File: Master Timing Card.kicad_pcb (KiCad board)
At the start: 4 copper layers, 170 x 100 mm, 412 parts, among them CN1 M20-9990346, CN10 M2 x 2.5mm, CN11 UE75-A20-6000T, CN12 U77-A1114-30L1, CN13 Harwin M20-9990246, CN14 USB4110-GF-A, CN15 731385033, CN2 Samtec GRF1-J-P-08-E-RA-TH1, CN3 Amphenol 86093488613755E1LF, CN6 SQW-104-01-F-D-VS, CN7 104031-0811, CN9 TE 1-2199230-6, J1 Connector_RJ45_Magjack_Abraco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, Q1 DMN62D0U-7, Q2 DMN62D0U-7, Q3 DMN62D0U-7, Q4 onsemi FDC6330L, Q5 TSM085P03CV RGG, Q6 DMN62D0U-7, T1 TC2-72T+, T2 TC2-72T+, T3 TC2-72T+, T4 TC2-72T+, T5 TC2-72T+, T6 TC2-72T+, T7 TC2-72T+, T8 TC2-72T+, T9 TC2-72T+, U1 Microchip 24LC024-E/MC, U10 INA3221AIRGV, U11 SY75576LKY, U12 TI TPS79301DBV, U13 LT3045IDD#PBF, U14 LT3045IDD#PBF, U15 SN74LVC1G02DCK, U2 Analog MAX3483ESA+, U3 TI TPS79301DBV, U4 TI TPS79301DBV, U5 RC32504A000GNK#BB0, U6 RC32504A000GNK#BB0, U7 SN74LVC1G125DBV, U8 SN74LVC1G125DBV, U9 Analog LT8650SEV#PBF

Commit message: schematic complete
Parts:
- removed C154, C156: 100n, Capacitor_SMD:C_0402_1005Metric
- removed CN1: M20-9990346, Connector_PinHeader_2.54mm:PinHeader_1x03_P2.54mm_Vertical
- removed FB1: 1k8, Inductor_SMD:L_0402_1005Metric
- removed R123, R124: 22k, Resistor_SMD:R_0402_1005Metric
- removed R125, R126: 4k7, Resistor_SMD:R_0402_1005Metric
- removed R127, R128, R132: 100R, Resistor_SMD:R_0402_1005Metric
- added C121: 100n, Capacitor_SMD:C_0402_1005Metric, F.Cu at (233.4, -18.0)
- added C144: 100n, Capacitor_SMD:C_0402_1005Metric, F.Cu at (233.4, -16.0)
- added C159: 100n, Capacitor_SMD:C_0402_1005Metric, F.Cu at (233.4, -14.0)
- added C160: 100n, Capacitor_SMD:C_0402_1005Metric, F.Cu at (246.4, -10.5)
- added C161: 100n, Capacitor_SMD:C_0402_1005Metric, F.Cu at (184.8, 102.8)
- added C162: 100n, Capacitor_SMD:C_0402_1005Metric, F.Cu at (184.8, 112.8)
- added C163: 100n, Capacitor_SMD:C_0402_1005Metric, F.Cu at (184.8, 114.8)
- added C164: 100n, Capacitor_SMD:C_0402_1005Metric, F.Cu at (184.8, 97.8)
- added C165: 100n, Capacitor_SMD:C_0402_1005Metric, F.Cu at (184.8, 99.8)
- added C166: 100n, Capacitor_SMD:C_0402_1005Metric, F.Cu at (184.8, 117.8)
- added C167: 100n, Capacitor_SMD:C_0402_1005Metric, F.Cu at (184.8, 119.8)
- added FB30: 1k8, Inductor_SMD:L_0402_1005Metric, F.Cu at (230.5, -18.0)
- added FB31: 1k8, Inductor_SMD:L_0402_1005Metric, F.Cu at (230.5, -16.0)
- added OSC1: 10MHz, Crystal:Crystal_SMD_3225-4Pin_3.2x2.5mm, F.Cu at (237.4, -16.7)
- added R133: 33R, Resistor_SMD:R_0402_1005Metric, F.Cu at (230.5, -14.0)
- added R134: 33R, Resistor_SMD:R_0402_1005Metric, F.Cu at (230.5, -12.0)
- added R135: 33R, Resistor_SMD:R_0402_1005Metric, F.Cu at (230.5, -10.0)
- added R136: 100R, Resistor_SMD:R_0402_1005Metric, F.Cu at (243.5, -2.50)
- added R137: 10k, Resistor_SMD:R_0402_1005Metric, F.Cu at (230.5, -8.01)
- added U16: SN74LVC2G157DCU, Package_SO:VSSOP-8_2.3x2mm_P0.5mm, F.Cu at (234.7, -11.3)
- R90: value 49R9 -> 100R
- R93: value 49R9 -> 10k
- U1: value Microchip 24LC024-E/MC -> DS2431P+; footprint Package_DFN_QFN:DFN-8-1EP_3x2mm_P0.5mm_EP1.36x1.46mm -> Package_SO_J-Lead:TSOC-6_3.76x3.94mm_P1.27mm
- moved LD9 282.1 mm to (47.7, 40.0), turned to -90 degrees
- moved U6 216.1 mm to (178.5, 111.2)
- moved T8 212.2 mm to (188.8, 118.8), turned to 90 degrees
- moved C111 205.1 mm to (184.8, 92.8), turned to 90 degrees
- moved C114 205.1 mm to (184.8, 94.8), turned to -90 degrees
- moved T7 203.8 mm to (188.8, 98.8), turned to 90 degrees
- moved CN15 202.5 mm to (40.0, 75.0), turned to -90 degrees
- moved C105 202.4 mm to (184.8, 104.8), turned to -90 degrees
- moved C108 202.3 mm to (184.8, 109.8), turned to -90 degrees
- moved T6 199.5 mm to (188.8, 113.8), turned to 90 degrees
- moved T5 192.2 mm to (188.8, 103.8), turned to 90 degrees
- moved R56 185.4 mm to (328.5, 36.7)
- moved C119 185.4 mm to (320.6, 26.1)
- moved C122 185.4 mm to (324.5, 33.9)
- moved LD1 185.4 mm to (338.2, 46.6)
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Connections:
- net /PLL and SFP/OE renamed /PLL and SFP/PLL_OE
- C105 pad 1: 0V -> /PLL and SFP/Frequency Synthesiser 2/RF1_P
- C108 pad 1: 0V -> /PLL and SFP/Frequency Synthesiser 2/RF2_N
- C111 pad 1: 0V -> /PLL and SFP/Frequency Synthesiser 1/RF3_P
- C114 pad 1: 0V -> /PLL and SFP/Frequency Synthesiser 1/RF3_N
- C12 pad 1: /GPS/GNSS_25MHZ -> /GPS/GNSS_CLK
- C153 pad 1: Net-(U13-EN/UV) -> /PLL and SFP/Frequency Synthesiser 1/VIN
- C155 pad 1: Net-(U14-EN/UV) -> /PLL and SFP/Frequency Synthesiser 2/VIN
- C23 pad 1: Net-(Q1-G) -> /GPS/GNSS_RESET
- C26 pad 1: 0V -> /PLL and SFP/Frequency Synthesiser 1/RF1_P
- C29 pad 1: 0V -> /PLL and SFP/Frequency Synthesiser 1/RF2_P
- C3 pad 1: Net-(U1-VCC) -> /PLL and SFP/Frequency Synthesiser 1/RF1_N
- C3 pad 2: 0V -> Net-(C3-Pad2)
- C32 pad 1: 0V -> /PLL and SFP/Frequency Synthesiser 1/RF2_N
- C35 pad 1: 0V -> /PLL and SFP/Frequency Synthesiser 2/RF2_P
- C57 pad 1: /PLL and SFP/Frequency Synthesiser 1/1v8_VDDREF -> /PLL and SFP/Frequency Synthesiser 1/1V8_VDDREF
- C58 pad 1: /PLL and SFP/Frequency Synthesiser 1/1v8_VDDREF -> /PLL and SFP/Frequency Synthesiser 1/1V8_VDDREF
- C83 pad 1: /PLL and SFP/Frequency Synthesiser 2/1v8_VDDREF -> /PLL and SFP/Frequency Synthesiser 2/1V8_VDDREF
- C90 pad 1: /PLL and SFP/Frequency Synthesiser 2/1v8_VDDREF -> /PLL and SFP/Frequency Synthesiser 2/1V8_VDDREF
- CN3 pad a1: Net-(CN3-Pada1) -> /RS485_B
- CN3 pad a10: 0V -> unconnected-(CN3-Pada10)
- CN3 pad a13: /SLOTS_EEPROM_3V3 -> unconnected-(CN3-Pada13)
- CN3 pad a14: /SLOTS_EEPROM_WP -> unconnected-(CN3-Pada14)
- CN3 pad a15: /PSU_EEPROM_SDA -> unconnected-(CN3-Pada15)
- CN3 pad a16: /PSU_EEPROM_ADDR2 -> 0V
- CN3 pad a2: Net-(CN3-Pada1) -> unconnected-(CN3-Pada2)
- CN3 pad a3: 0V -> unconnected-(CN3-Pada3)
- CN3 pad a4: Net-(CN3-Pada4) -> unconnected-(CN3-Pada4)
- CN3 pad a5: Net-(CN3-Pada4) -> unconnected-(CN3-Pada5)
- CN3 pad a6: 0V -> unconnected-(CN3-Pada6)
- CN3 pad a7: Net-(CN3-Pada7) -> unconnected-(CN3-Pada7)
- CN3 pad a8: Net-(CN3-Pada7) -> unconnected-(CN3-Pada8)
- CN3 pad a9: 0V -> unconnected-(CN3-Pada9)
- CN3 pad b1: unconnected-(CN3-Padb1) -> /RS485_A
- CN3 pad b10: 0V -> unconnected-(CN3-Padb10)
- CN3 pad b13: /SLOTS_EEPROM_SDA -> unconnected-(CN3-Padb13)
- CN3 pad b14: /SLOTS_EEPROM_SCL -> unconnected-(CN3-Padb14)
- CN3 pad b15: /PSU_EEPROM_SCL -> unconnected-(CN3-Padb15)
- CN3 pad b16: /PSU_EEPROM_ADDR1 -> unconnected-(CN3-Padb16)
- CN3 pad b3: 0V -> unconnected-(CN3-Padb3)
- CN3 pad b4: Net-(CN3-Padb4) -> unconnected-(CN3-Padb4)
- CN3 pad b5: Net-(CN3-Padb4) -> unconnected-(CN3-Padb5)
- CN3 pad b6: 0V -> unconnected-(CN3-Padb6)
- CN3 pad b7: Net-(CN3-Padb7) -> unconnected-(CN3-Padb7)
- CN3 pad b8: Net-(CN3-Padb7) -> unconnected-(CN3-Padb8)
- CN3 pad b9: 0V -> unconnected-(CN3-Padb9)
- CN3 pad c1: Net-(CN3-Padc1) -> Net-(U1-IO)
- CN3 pad c10: 0V -> unconnected-(CN3-Padc10)
- CN3 pad c13: /RS485_B -> unconnected-(CN3-Padc13)
- CN3 pad c14: /RS485_A -> unconnected-(CN3-Padc14)
- CN3 pad c15: /PSU_EEPROM_3V3 -> unconnected-(CN3-Padc15)
- CN3 pad c16: /PSU_EEPROM_ADDR0 -> unconnected-(CN3-Padc16)
- CN3 pad c2: Net-(CN3-Padc1) -> unconnected-(CN3-Padc2)
- CN3 pad c3: 0V -> unconnected-(CN3-Padc3)
- CN3 pad c4: Net-(CN3-Padc4) -> unconnected-(CN3-Padc4)
- CN3 pad c5: Net-(CN3-Padc4) -> unconnected-(CN3-Padc5)
- CN3 pad c6: 0V -> unconnected-(CN3-Padc6)
- CN3 pad c7: Net-(CN3-Padc7) -> unconnected-(CN3-Padc7)
- CN3 pad c8: Net-(CN3-Padc7) -> unconnected-(CN3-Padc8)
- CN3 pad c9: 0V -> unconnected-(CN3-Padc9)
- CN4 pad 24: unconnected-(CN4D-GPIO26-Pad24) -> Net-(CN4D-GPIO26)
- CN4 pad 48: unconnected-(CN4D-GPIO27-Pad48) -> Net-(CN4D-GPIO27)
- CN6 pad 7: /GPS/GNSS_25MHZ -> /GPS/GNSS_CLK
- CN7 pad 10: unconnected-(CN7-DET_A-Pad10) -> 0V
- FB13 pad 2: /PLL and SFP/Frequency Synthesiser 1/1v8_VDDREF -> /PLL and SFP/Frequency Synthesiser 1/1V8_VDDREF
- FB21 pad 2: /PLL and SFP/Frequency Synthesiser 2/1v8_VDDREF -> /PLL and SFP/Frequency Synthesiser 2/1V8_VDDREF
- FB28 pad 2: Net-(U13-EN/UV) -> /PLL and SFP/Frequency Synthesiser 1/VIN
- FB29 pad 2: Net-(U14-EN/UV) -> /PLL and SFP/Frequency Synthesiser 2/VIN
- FB5 pad 2: /GPS/GNSS_25MHZ -> /GPS/GNSS_CLK
- Q1 pad 1: Net-(Q1-G) -> /GPS/GNSS_RESET
- R17 pad 1: /GPS/GNSS_25MHZ -> Net-(U16-B)
- R24 pad 1: /GPS/GNSS_RESET -> Net-(CN4D-GPIO26)
- R24 pad 2: Net-(Q1-G) -> /GPS/CLK_SEL
- R25 pad 1: Net-(Q1-G) -> /GPS/GNSS_RESET
- R90 pad 1: Net-(U11-IN1_N) -> /GPS/REF_CLK_P
- R90 pad 2: 0V -> /GPS/REF_CLK_N
- R93 pad 1: Net-(U11-IN1_P) -> /PLL and SFP/CLK_SEL
- T1 pad 1: Net-(U5-OUT0_P) -> Net-(C26-Pad2)
- T1 pad 2: Net-(C26-Pad2) -> 0V
- T1 pad 3: Net-(U5-OUT0_N) -> Net-(C3-Pad2)
- T2 pad 1: Net-(U5-OUT1_N) -> Net-(C32-Pad2)
- T2 pad 2: Net-(C29-Pad2) -> 0V
- T2 pad 3: Net-(U5-OUT1_P) -> Net-(C29-Pad2)
- T3 pad 1: Net-(U5-OUT2_N) -> Net-(C108-Pad2)
- T3 pad 2: Net-(C32-Pad2) -> 0V
- T3 pad 3: Net-(U5-OUT2_P) -> Net-(C35-Pad2)
- T3 pad 4: /RF3 -> /RF6
- T4 pad 1: Net-(U5-OUT3_N) -> Net-(C114-Pad2)
- T4 pad 2: Net-(C35-Pad2) -> 0V
- T4 pad 3: Net-(U5-OUT3_P) -> Net-(C111-Pad2)
- T4 pad 4: /RF4 -> /RF3
- T5 pad 1: Net-(U6-OUT0_P) -> Net-(C105-Pad2)
- T5 pad 2: Net-(C105-Pad2) -> 0V
- T5 pad 3: Net-(U6-OUT0_N) -> Net-(C161-Pad2)
- T6 pad 1: Net-(U6-OUT1_N) -> Net-(C163-Pad2)
- T6 pad 2: Net-(C108-Pad2) -> 0V
- T6 pad 3: Net-(U6-OUT1_P) -> Net-(C162-Pad2)
- T6 pad 4: /RF6 -> /RF7
- T7 pad 1: Net-(U6-OUT2_N) -> Net-(C165-Pad2)
- T7 pad 2: Net-(C111-Pad2) -> 0V
- T7 pad 3: Net-(U6-OUT2_P) -> Net-(C164-Pad2)
- T7 pad 4: /RF7 -> /RF4
- T8 pad 1: Net-(U6-OUT3_N) -> Net-(C167-Pad2)
- T8 pad 2: Net-(C114-Pad2) -> 0V
- T8 pad 3: Net-(U6-OUT3_P) -> Net-(C166-Pad2)
- U1 pad 1: /PSU_EEPROM_ADDR0 -> 0V
- U1 pad 2: /PSU_EEPROM_ADDR1 -> Net-(U1-IO)
- U1 pad 3: /PSU_EEPROM_ADDR2 -> unconnected-(U1-NC-Pad3)
- U1 pad 4: 0V -> unconnected-(U1-NC-Pad4)
- U1 pad 5: /PSU_EEPROM_SDA -> unconnected-(U1-NC-Pad5)
- U1 pad 6: /PSU_EEPROM_SCL -> unconnected-(U1-NC-Pad6)
- U11 pad 1: unconnected-(U11-SEL-Pad1) -> /PLL and SFP/CLK_SEL
- U11 pad 3: Net-(U11-IN1_P) -> /GPS/REF_CLK_P
- U11 pad 4: Net-(U11-IN1_N) -> /GPS/REF_CLK_N
- U13 pad 1: Net-(U13-EN/UV) -> /PLL and SFP/Frequency Synthesiser 1/VIN
- U13 pad 2: Net-(U13-EN/UV) -> /PLL and SFP/Frequency Synthesiser 1/VIN
- U13 pad 3: Net-(U13-EN/UV) -> /PLL and SFP/Frequency Synthesiser 1/VIN
- U13 pad 4: Net-(U13-PG) -> unconnected-(U13-PG-Pad4)
- U13 pad 6: Net-(U13-PGFB) -> /PLL and SFP/Frequency Synthesiser 1/VIN
- U14 pad 1: Net-(U14-EN/UV) -> /PLL and SFP/Frequency Synthesiser 2/VIN
- U14 pad 2: Net-(U14-EN/UV) -> /PLL and SFP/Frequency Synthesiser 2/VIN
- U14 pad 3: Net-(U14-EN/UV) -> /PLL and SFP/Frequency Synthesiser 2/VIN
- U14 pad 4: Net-(U14-PG) -> unconnected-(U14-PG-Pad4)
- U14 pad 6: Net-(U14-PGFB) -> /PLL and SFP/Frequency Synthesiser 2/VIN
- U5 pad 11: Net-(U5-OUT3_N) -> /PLL and SFP/Frequency Synthesiser 1/RF4_N
- U5 pad 12: Net-(U5-OUT3_P) -> /PLL and SFP/Frequency Synthesiser 1/RF4_P
- U5 pad 14: Net-(U5-OUT2_N) -> /PLL and SFP/Frequency Synthesiser 1/RF3_N
- U5 pad 15: Net-(U5-OUT2_P) -> /PLL and SFP/Frequency Synthesiser 1/RF3_P
- U5 pad 17: Net-(U5-OUT1_N) -> /PLL and SFP/Frequency Synthesiser 1/RF2_N
- U5 pad 18: Net-(U5-OUT1_P) -> /PLL and SFP/Frequency Synthesiser 1/RF2_P
- U5 pad 20: Net-(U5-OUT0_P) -> /PLL and SFP/Frequency Synthesiser 1/RF1_P
- U5 pad 21: Net-(U5-OUT0_N) -> /PLL and SFP/Frequency Synthesiser 1/RF1_N
- U6 pad 11: Net-(U6-OUT3_N) -> /PLL and SFP/Frequency Synthesiser 2/RF4_N
- U6 pad 12: Net-(U6-OUT3_P) -> /PLL and SFP/Frequency Synthesiser 2/RF4_P
- U6 pad 14: Net-(U6-OUT2_N) -> /PLL and SFP/Frequency Synthesiser 2/RF3_N
- U6 pad 15: Net-(U6-OUT2_P) -> /PLL and SFP/Frequency Synthesiser 2/RF3_P
- U6 pad 17: Net-(U6-OUT1_N) -> /PLL and SFP/Frequency Synthesiser 2/RF2_N
- U6 pad 18: Net-(U6-OUT1_P) -> /PLL and SFP/Frequency Synthesiser 2/RF2_P
- U6 pad 20: Net-(U6-OUT0_P) -> /PLL and SFP/Frequency Synthesiser 2/RF1_P
- U6 pad 21: Net-(U6-OUT0_N) -> /PLL and SFP/Frequency Synthesiser 2/RF1_N
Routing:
- net 0V: track 4.10 -> 45.6 mm, vias 8 -> 37
- net /PSU_EEPROM_SCL: track 12.5 -> 0.00 mm
- net /PLL and SFP/Frequency Synthesiser 1/RF1_N: track 0.00 -> 10.6 mm
- net Net-(U5-OUT0_N): track 10.5 -> 0.00 mm
- net /PSU_EEPROM_ADDR1: track 10.2 -> 0.00 mm
- net /PLL and SFP/Frequency Synthesiser 1/RF1_P: track 0.00 -> 9.85 mm
- net /PLL and SFP/Frequency Synthesiser 1/RF4_N: track 0.00 -> 9.61 mm
- net /PSU_EEPROM_ADDR0: track 9.58 -> 0.00 mm
- net /PLL and SFP/Frequency Synthesiser 1/RF4_P: track 0.00 -> 8.91 mm
- net Net-(U5-OUT0_P): track 8.52 -> 0.00 mm
- net /PSU_EEPROM_3V3: track 7.14 -> 0.00 mm, vias 1 -> 0
- net /PSU_EEPROM_SDA: track 6.87 -> 0.00 mm
- net Net-(U1-WP): track 6.55 -> 0.00 mm
- net /PLL and SFP/Frequency Synthesiser 1/RF3_P: track 0.00 -> 5.64 mm
- net /PLL and SFP/Frequency Synthesiser 1/RF3_N: track 0.00 -> 5.64 mm
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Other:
- outline, holes or cut-outs redrawn
- board text added: "Space for GPS SMA"
- board text added: "Use JLC04161H-7628 Stackup"

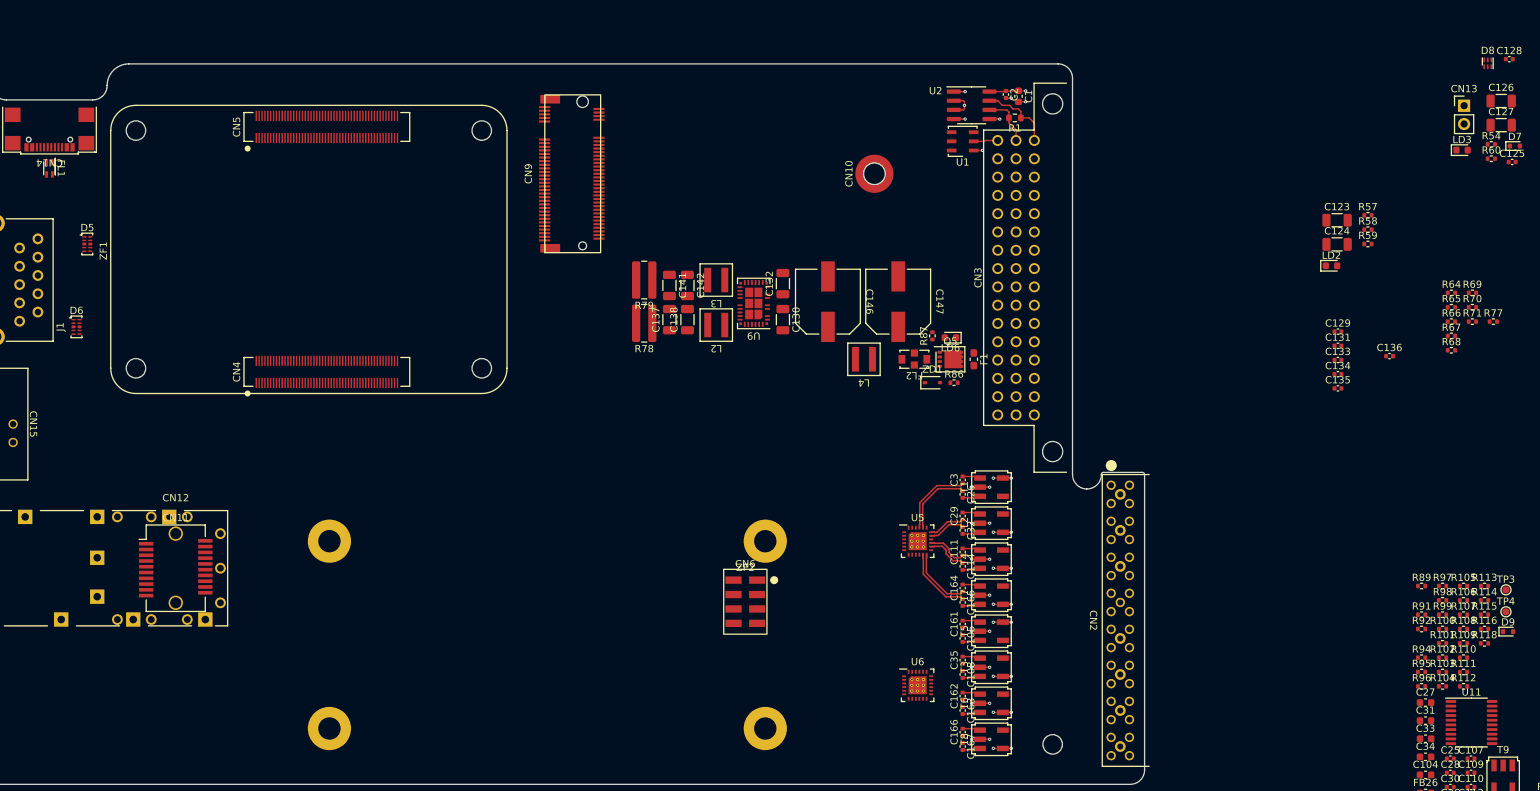
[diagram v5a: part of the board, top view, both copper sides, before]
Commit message: Moved to preferred library
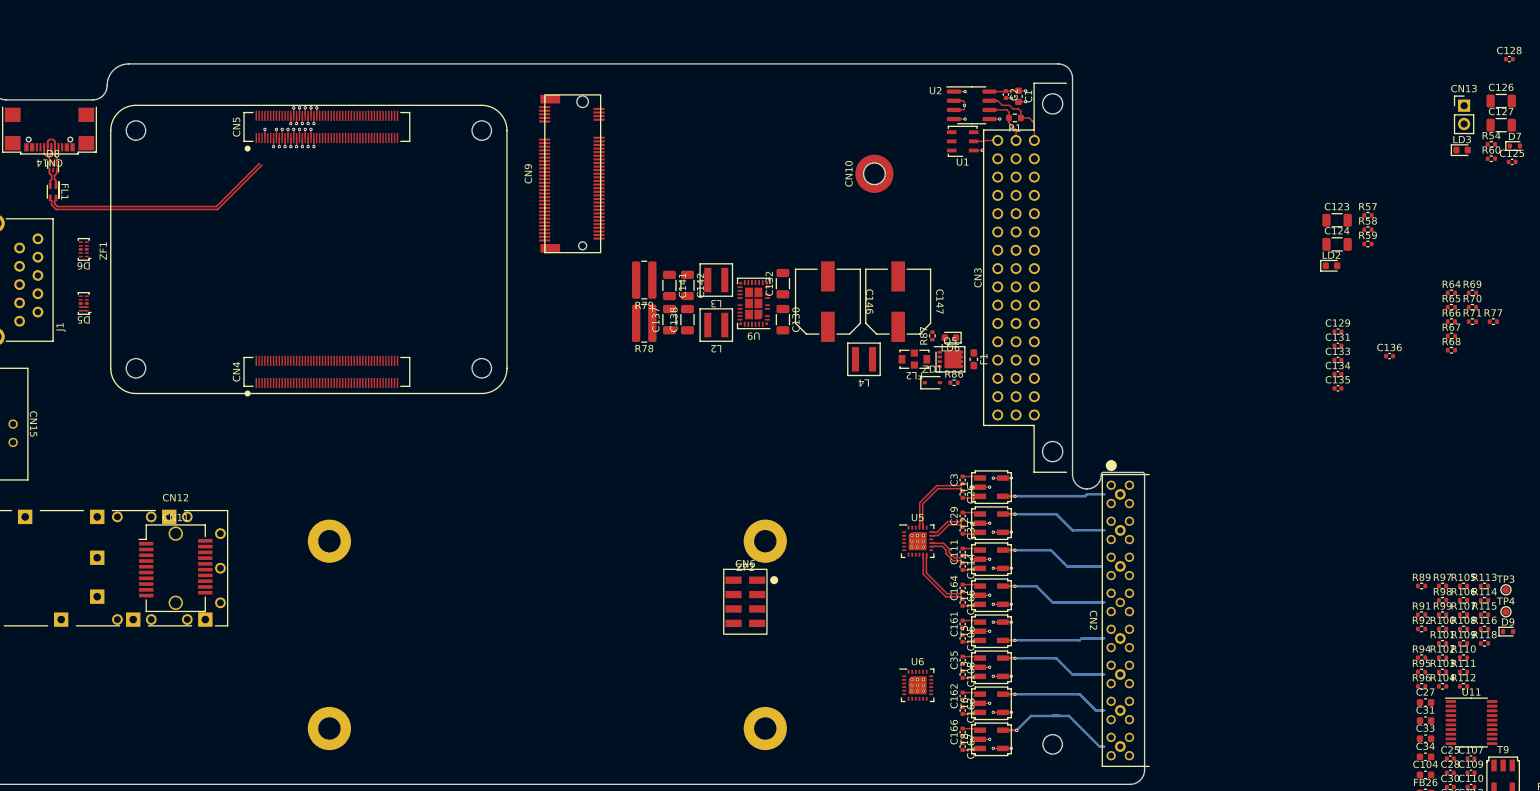
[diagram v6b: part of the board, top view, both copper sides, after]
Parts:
- moved D8 199.7 mm to (58.5, 39.2)
- moved D6 10.8 mm to (62.8, 50.8), turned to 180 degrees
- moved D5 8.27 mm to (62.8, 58.2), turned to 180 degrees
- moved FL1 3.29 mm to (58.5, 42.8)
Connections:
- net Net-(CN4B-Ethernet_Pair0_N) renamed /CM4 Interfaces/ETHA_N
- net Net-(CN4B-Ethernet_Pair0_P) renamed /CM4 Interfaces/ETHA_P
- net Net-(CN4B-Ethernet_Pair1_N) renamed /CM4 Interfaces/ETHB_N
- net Net-(CN4B-Ethernet_Pair1_P) renamed /CM4 Interfaces/ETHB_P
- net Net-(CN4B-Ethernet_Pair2_N) renamed /CM4 Interfaces/ETHC_N
- net Net-(CN4B-Ethernet_Pair2_P) renamed /CM4 Interfaces/ETHC_P
- net Net-(CN4B-Ethernet_Pair3_N) renamed /CM4 Interfaces/ETHD_N
- net Net-(CN4B-Ethernet_Pair3_P) renamed /CM4 Interfaces/ETHD_P
- CN14 pad A6: Net-(CN14-DP1) -> /Pi CM4 - HPIO/USB_P
- CN14 pad A7: Net-(CN14-DN1) -> /Pi CM4 - HPIO/USB_N
- CN14 pad B6: Net-(CN14-DP1) -> /Pi CM4 - HPIO/USB_P
- CN14 pad B7: Net-(CN14-DN1) -> /Pi CM4 - HPIO/USB_N
- CN5 pad 103: Net-(CN5A-USB2_N) -> /Pi CM4 - HPIO/D_N
- CN5 pad 105: Net-(CN5A-USB2_P) -> /Pi CM4 - HPIO/D_P
- D8 pad 1: Net-(CN14-DP1) -> /Pi CM4 - HPIO/USB_P
- D8 pad 3: Net-(CN14-DN1) -> /Pi CM4 - HPIO/USB_N
- D8 pad 4: Net-(CN14-DN1) -> /Pi CM4 - HPIO/USB_N
- D8 pad 6: Net-(CN14-DP1) -> /Pi CM4 - HPIO/USB_P
- FL1 pad 1: Net-(CN14-DP1) -> /Pi CM4 - HPIO/USB_N
- FL1 pad 2: Net-(CN5A-USB2_P) -> /Pi CM4 - HPIO/D_N
- FL1 pad 3: Net-(CN14-DN1) -> /Pi CM4 - HPIO/USB_P
- FL1 pad 4: Net-(CN5A-USB2_N) -> /Pi CM4 - HPIO/D_P
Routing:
- net /Pi CM4 - HPIO/D_P: track 0.00 -> 33.1 mm
- net /Pi CM4 - HPIO/D_N: track 0.00 -> 31.9 mm
- net 0V: track 45.6 -> 75.8 mm, vias 37 -> 63
- net /RF8: track 0.00 -> 17.7 mm, vias 0 -> 1
- net /RF7: track 0.00 -> 15.0 mm, vias 0 -> 1
- net /RF6: track 0.00 -> 15.0 mm, vias 0 -> 1
- net /RF4: track 0.00 -> 15.0 mm, vias 0 -> 1
- net /RF2: track 0.00 -> 15.0 mm, vias 0 -> 1
- net /RF3: track 0.00 -> 14.6 mm, vias 0 -> 1
- net /RF5: track 0.00 -> 14.2 mm, vias 0 -> 1
- net /RF1: track 0.00 -> 14.2 mm, vias 0 -> 1
- net /Pi CM4 - HPIO/USB_N: track 0.00 -> 7.54 mm
- net /Pi CM4 - HPIO/USB_P: track 0.00 -> 6.46 mm
- net /CM4 Interfaces/ETHA_P: track 0.00 -> 0.83 mm
- net /CM4 Interfaces/ETHA_N: track 0.00 -> 0.83 mm

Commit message: Started placement
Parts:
- removed C33: 10u, Capacitor_SMD:C_0603_1608Metric
- removed L1: 4u7, Inductor_SMD:L_1210_3225Metric
- added H8: ~, Misc_WUT:Logo_10mmx10mm, F.Cu at (52.8, 115.0)
- C19: footprint Capacitor_SMD:C_0603_1608Metric -> Capacitor_SMD:C_0402_1005Metric
- C20: value 68u -> 10u; footprint Capacitor_WUT:Wurth_WCAP_PSHP_8x8.7mm_SM -> Capacitor_SMD:C_0603_1608Metric
- C24: value 4n7 -> 100n; footprint Capacitor_SMD:C_0603_1608Metric -> Capacitor_SMD:C_0402_1005Metric
- C4: value 10u -> 4n7; footprint Capacitor_SMD:C_0603_1608Metric -> Capacitor_SMD:C_0402_1005Metric
- U10: footprint IC_WUT:Texas_VFQN-16-1EP_RGV0016A -> IC_WUT:Texas_VQFN-16-1EP_RGV0016A
- moved R39 367.9 mm to (53.0, 43.0), turned to 180 degrees
- moved R45 325.5 mm to (95.8, 72.2), turned to -90 degrees
- moved R38 323.2 mm to (53.0, 44.2), turned to 180 degrees
- moved C116 322.9 mm to (105.8, 79.0)
- moved C117 322.8 mm to (105.8, 84.0), turned to -90 degrees
- moved D1 322.2 mm to (103.0, 79.0), turned to 180 degrees
- moved Q4 322.0 mm to (103.0, 83.5), turned to 180 degrees
- moved R43 320.9 mm to (98.0, 72.2), turned to -90 degrees
- moved R49 320.6 mm to (100.2, 83.5), turned to -90 degrees
- moved R51 319.7 mm to (102.0, 72.2), turned to 90 degrees
- moved R40 319.5 mm to (99.0, 72.2), turned to -90 degrees
- moved R41 318.6 mm to (100.0, 72.2), turned to -90 degrees
- moved R50 317.9 mm to (103.0, 86.0)
- moved R42 317.8 mm to (101.0, 72.2), turned to -90 degrees
- moved C39 288.6 mm to (140.2, 97.2), turned to 90 degrees
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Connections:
- net /GPS/GNSS_CLK renamed /GPS/GNSS_CLK_M
- net Net-(C130-Pad1) renamed /Power Supplies/12V_DCDC
- net Net-(C147-Pad1) renamed /Power Supplies/12V_FILT
- net Net-(F1-Pad2) renamed /Power Supplies/12V_F
- net Net-(L2-Pad1) renamed /Power Supplies/SW1
- net Net-(L3-Pad1) renamed /Power Supplies/SW2
- net Net-(ZD1-K) renamed /Power Supplies/12V_PROT
- C11 pad 1: /GPS/GNSS_PPS -> /GPS/GNSS_PPS_M
- C24 pad 1: /GPS/~{GNSS_RESET} -> Net-(U11-VDD)
- C4 pad 1: 5V0_PI -> /GPS/~{GNSS_RESET_M}
- C5 pad 1: /GPS/GNSS_TX -> /GPS/GNSS_TX_M
- C6 pad 1: /GPS/GNSS_RX -> /GPS/GNSS_RX_M
- C7 pad 1: Net-(U3-EN) -> 5V0_PI
- C8 pad 1: Net-(U3-EN) -> 5V0_PI
- CN6 pad 3: /GPS/GNSS_TX -> /GPS/GNSS_TX_M
- CN6 pad 4: /GPS/~{GNSS_RESET} -> /GPS/~{GNSS_RESET_M}
- CN6 pad 5: /GPS/GNSS_RX -> /GPS/GNSS_RX_M
- CN6 pad 6: /GPS/GNSS_PPS -> /GPS/GNSS_PPS_M
- D3 pad 1: /Pi CM4 - HPIO/PCIE_PER0_P -> /Pi CM4 - HPIO/PCIE_PER0_N
- D3 pad 10: /Pi CM4 - HPIO/PCIE_PER0_P -> /Pi CM4 - HPIO/PCIE_PER0_N
- D3 pad 2: /Pi CM4 - HPIO/PCIE_PER0_N -> /Pi CM4 - HPIO/PCIE_PER0_P
- D3 pad 4: /Pi CM4 - HPIO/PCIE_PET0_P -> /Pi CM4 - HPIO/PCIE_PET0_N
- D3 pad 5: /Pi CM4 - HPIO/PCIE_PET0_N -> /Pi CM4 - HPIO/PCIE_PET0_P
- D3 pad 6: /Pi CM4 - HPIO/PCIE_PET0_N -> /Pi CM4 - HPIO/PCIE_PET0_P
- D3 pad 7: /Pi CM4 - HPIO/PCIE_PET0_P -> /Pi CM4 - HPIO/PCIE_PET0_N
- D3 pad 9: /Pi CM4 - HPIO/PCIE_PER0_N -> /Pi CM4 - HPIO/PCIE_PER0_P
- FB2 pad 1: /GPS/GNSS_RX -> Net-(FB2-Pad1)
- FB2 pad 2: /GPS/GNSS_TX -> /GPS/GNSS_TX_M
- FB3 pad 1: Net-(FB3-Pad1) -> /GPS/GNSS_TX
- FB3 pad 2: /GPS/GNSS_RX -> /GPS/GNSS_RX_M
- FB4 pad 2: /GPS/GNSS_PPS -> /GPS/GNSS_PPS_M
- R135 pad 1: Net-(U16-A) -> Net-(U16-B)
- R17 pad 1: Net-(U16-B) -> Net-(U16-A)
- R18 pad 1: /GPS/GNSS_TX -> Net-(FB2-Pad1)
- R18 pad 2: Net-(FB3-Pad1) -> /GPS/GNSS_RX
- R26 pad 2: /GPS/~{GNSS_RESET} -> /GPS/~{GNSS_RESET_M}
- R27 pad 2: /GPS/~{GNSS_RESET} -> /GPS/~{GNSS_RESET_M}
- U3 pad 1: Net-(U3-EN) -> 5V0_PI
- U3 pad 3: Net-(U3-EN) -> 5V0_PI
- U4 pad 1: Net-(U3-EN) -> 5V0_PI
- U4 pad 3: Net-(U3-EN) -> 5V0_PI
- U9 pad 26: 5V0_PI -> unconnected-(U9-BIAS-Pad26)
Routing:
- net 0V: track 75.8 -> 144.8 mm, vias 63 -> 137
- net /Pi CM4 - HPIO/PCIE_PET0_P: track 0.00 -> 45.8 mm
- net /Pi CM4 - HPIO/PCIE_PET0_N: track 0.00 -> 45.2 mm
- net /CM4 Interfaces/SD_PWR_ON: track 0.00 -> 25.2 mm, vias 0 -> 2
- net Net-(CN7-DAT2): track 0.00 -> 21.2 mm, vias 0 -> 2
- net Net-(CN7-DAT1): track 0.00 -> 20.7 mm, vias 0 -> 2
- net Net-(CN7-DAT0): track 0.00 -> 20.5 mm, vias 0 -> 2
- net Net-(CN7-CMD): track 0.00 -> 20.1 mm, vias 0 -> 2
- net Net-(CN7-DAT3/CD): track 0.00 -> 19.8 mm, vias 0 -> 2
- net Net-(CN7-CLK): track 0.00 -> 19.8 mm, vias 0 -> 2
- net Net-(C128-Pad2): track 0.00 -> 16.9 mm, vias 0 -> 4
- net /CM4 Interfaces/SD_CLK: track 0.00 -> 12.1 mm
- net Net-(CN14-CC1): track 0.00 -> 11.5 mm, vias 0 -> 2
- net /CM4 Interfaces/SD_DAT0: track 0.00 -> 11.4 mm, vias 0 -> 2
- net 3V3: track 5.09 -> 15.8 mm, vias 1 -> 5
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- added copper zone on F.Cu, net /Power Supplies/12V_DCDC
- added copper zone on F.Cu, net /Power Supplies/12V_FILT
- added copper zone on F.Cu, net 0V
- added copper zone on F.Cu, net 3V3_PCIE

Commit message: moving to discrete GPS recevier
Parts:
- removed CN6: SQW-104-01-F-D-VS, Connector_WUT:Samtec_SQW-104-01
- removed R109, R113, R114: 180R, Resistor_SMD:R_0402_1005Metric
- removed R112: 140R, Resistor_SMD:R_0402_1005Metric
- removed ZF2: u-blox RCB-F9T, RF_WUT:u-blox_RCB-F9T
- added C154: 100n, Capacitor_SMD:C_0402_1005Metric, F.Cu at (145.2, 73.5)
- added C33: 100n, Capacitor_SMD:C_0402_1005Metric, F.Cu at (149.2, 77.0)
- added SH1: MS585-10F, Shield_WUT:Shield_Masach_MS585-10_58.2x49.4x4.7mm_SMD, F.Cu at (156.8, 96.0)
- added U17: ZED-F9T-10B, RF_WUT:uBlox_ZED, F.Cu at (57.7, 110.5)
- R107: value 140R -> 82R
- R108: value 180R -> 82R
- R91, R92: value 49R9 -> 130R
- moved R13 344.0 mm to (26.0, 29.2), turned to 180 degrees
- moved R12 343.8 mm to (26.0, 33.0), turned to 180 degrees
- moved R11 343.8 mm to (26.0, 31.8), turned to 180 degrees
- moved R10 343.8 mm to (26.0, 30.5), turned to 180 degrees
- moved D9 303.6 mm to (56.5, 76.2), turned to -90 degrees
- moved T9 295.4 mm to (66.2, 74.2), turned to -90 degrees
- moved R98 289.7 mm to (58.5, 75.5)
- moved C112 289.3 mm to (70.2, 79.0), turned to 90 degrees
- moved C109 288.0 mm to (68.2, 79.0), turned to 90 degrees
- moved R99 287.8 mm to (60.2, 76.0), turned to -90 degrees
- moved C110 286.9 mm to (69.2, 79.0), turned to 90 degrees
- moved Q6 286.6 mm to (72.5, 78.0), turned to -90 degrees
- moved C113 286.5 mm to (72.5, 75.5), turned to 180 degrees
- moved R97 286.5 mm to (62.0, 75.5), turned to 180 degrees
- moved R118 284.2 mm to (72.5, 74.5), turned to 180 degrees
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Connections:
- net Net-(CN11-RD+) renamed /PLL and SFP/REFCLK_R_N
- net Net-(CN11-RD-) renamed /PLL and SFP/REFCLK_R_P
- net Net-(U11-CLKA_N) renamed /PLL and SFP/CLKA_N
- net Net-(U11-CLKA_P) renamed /PLL and SFP/CLKA_P
- net Net-(U11-CLKB_N) renamed /PLL and SFP/CLKB_N
- net Net-(U11-CLKB_P) renamed /PLL and SFP/CLKB_P
- net Net-(U11-CLKC_N) renamed /PLL and SFP/CLKC_N
- net Net-(U11-CLKC_P) renamed /PLL and SFP/CLKC_P
- net Net-(U11-CLKD_N) renamed /PLL and SFP/CLKD_N
- net Net-(U11-CLKD_P) renamed /PLL and SFP/CLKD_P
- C24 pad 1: Net-(U11-VDD) -> /PLL and SFP/VDD_MUX
- C30 pad 1: Net-(U11-VDD) -> /PLL and SFP/VDD_MUX
- C31 pad 1: Net-(U11-VDD) -> /PLL and SFP/VDD_MUX
- R107 pad 1: /PLL and SFP/PLL1_CLK_P -> /PLL and SFP/SFP_REFCLK_P
- R107 pad 2: /PLL and SFP/PLL1_CLK_N -> 0V
- R108 pad 1: 0V -> /PLL and SFP/SFP_REFCLK_N
- R108 pad 2: /PLL and SFP/PLL1_CLK_P -> 0V
- R115 pad 1: Net-(U11-VDD) -> /PLL and SFP/VDD_MUX
- R91 pad 1: /PLL and SFP/SFP_REFCLK_P -> /PLL and SFP/VDD_MUX
- R91 pad 2: 0V -> /PLL and SFP/SFP_REFCLK_P
- R92 pad 1: /PLL and SFP/SFP_REFCLK_N -> /PLL and SFP/VDD_MUX
- R92 pad 2: 0V -> /PLL and SFP/SFP_REFCLK_N
- TP3 pad 1: Net-(U11-VDD) -> /PLL and SFP/VDD_MUX
- U11 pad 15: Net-(U11-VDD) -> /PLL and SFP/VDD_MUX
- U11 pad 2: Net-(U11-VDD) -> /PLL and SFP/VDD_MUX
- U11 pad 3: /GPS/REF_CLK_P -> /PLL and SFP/SFP_REFCLK_P
- U11 pad 4: /GPS/REF_CLK_N -> /PLL and SFP/SFP_REFCLK_N
- U11 pad 6: /PLL and SFP/SFP_REFCLK_P -> /GPS/REF_CLK_P
- U11 pad 7: /PLL and SFP/SFP_REFCLK_N -> /GPS/REF_CLK_N
- U12 pad 6: Net-(U11-VDD) -> /PLL and SFP/VDD_MUX
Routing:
- net 0V: track 144.8 -> 201.6 mm, vias 137 -> 196
- net /Pi CM4 - HPIO/D_P: track 33.1 -> 0.00 mm
- net /Pi CM4 - HPIO/D_N: track 31.9 -> 0.00 mm
- net Net-(CN11-VccT): track 0.00 -> 21.8 mm, vias 0 -> 2
- net Net-(CN11-VccR): track 0.00 -> 18.2 mm, vias 0 -> 2
- net /PLL and SFP/VDD_MUX: track 0.00 -> 12.5 mm, vias 0 -> 3
- net Net-(U3-OUT): track 0.00 -> 10.2 mm
- net /GPS/VCC_GNSS: track 0.00 -> 8.58 mm
- net /PLL and SFP/SFP_REFCLK_N: track 0.00 -> 7.67 mm
- net /PLL and SFP/SFP_REFCLK_P: track 0.00 -> 7.67 mm
- net /GPS/REF_CLK_N: track 0.00 -> 7.54 mm
- net Net-(U5-XIN/REF): track 0.00 -> 7.33 mm
- net /GPS/REF_CLK_P: track 0.00 -> 7.28 mm
- net Net-(C34-Pad1): track 0.00 -> 6.11 mm
- net Net-(U4-OUT): track 0.00 -> 6.10 mm
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- removed copper zone on F.Cu, net /Power Supplies/12V_DCDC
- removed copper zone on F.Cu, net /Power Supplies/12V_FILT
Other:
- board text removed: "Space for GPS SMA"
